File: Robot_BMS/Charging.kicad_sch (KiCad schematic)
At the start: 18 parts, among them Q7 2N7002, Q8 2N7002, Q9 2N7002, U4 MCP73833-xxx-MF, U5 MCP73833-xxx-MF, U6 MCP73833-xxx-MF

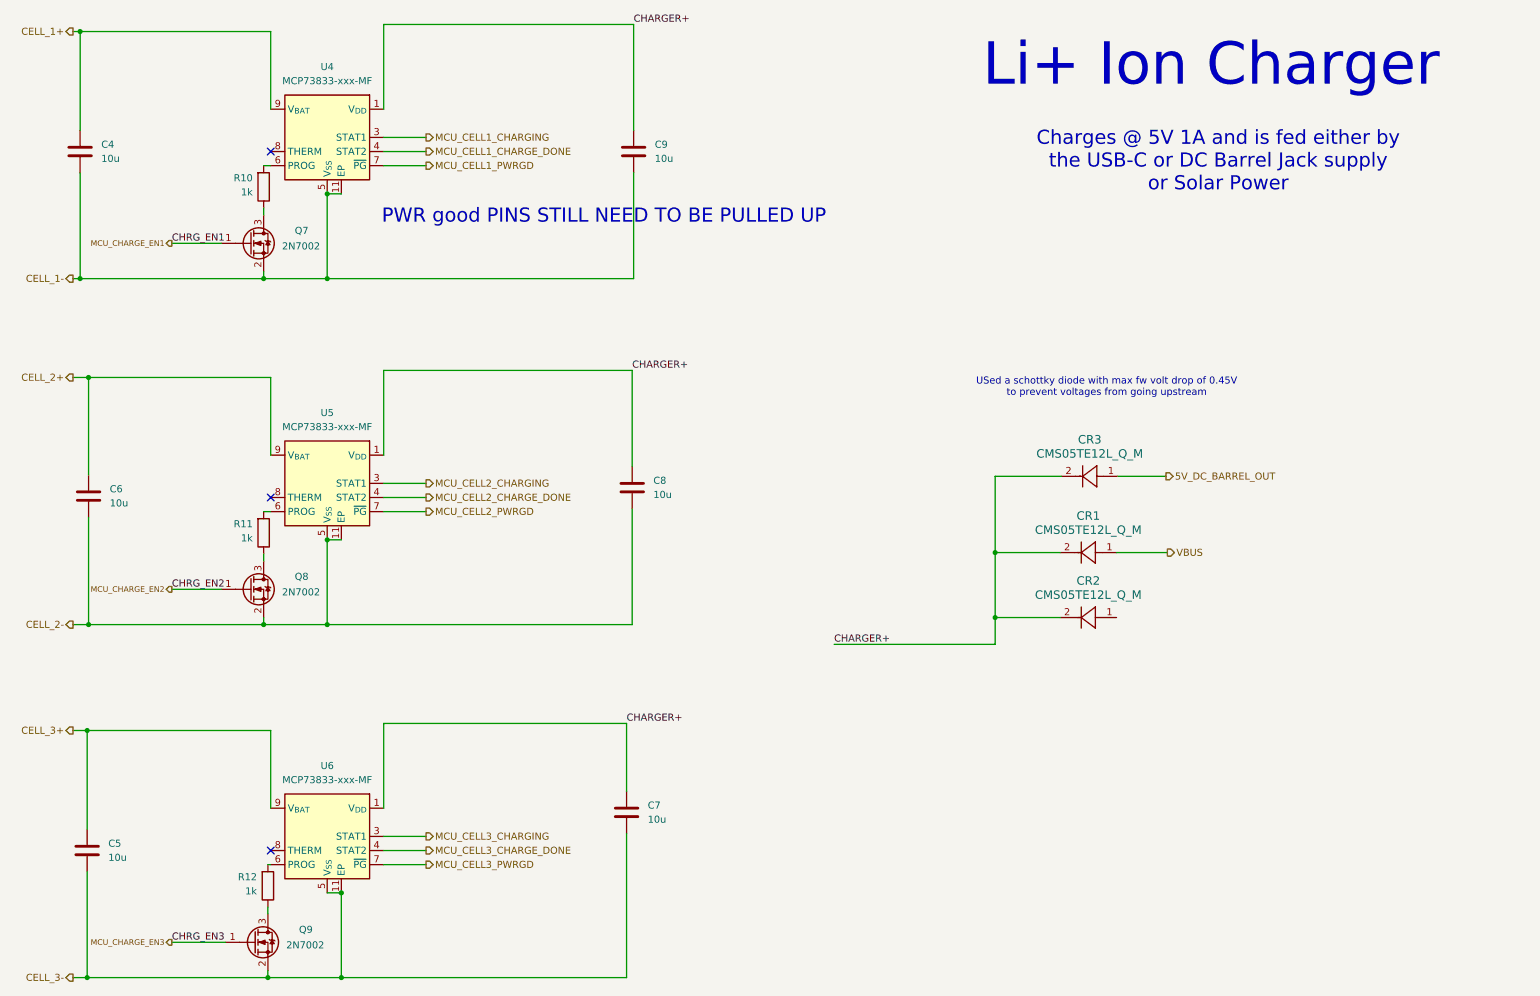
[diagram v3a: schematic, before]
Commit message: USB-c PD to 15V
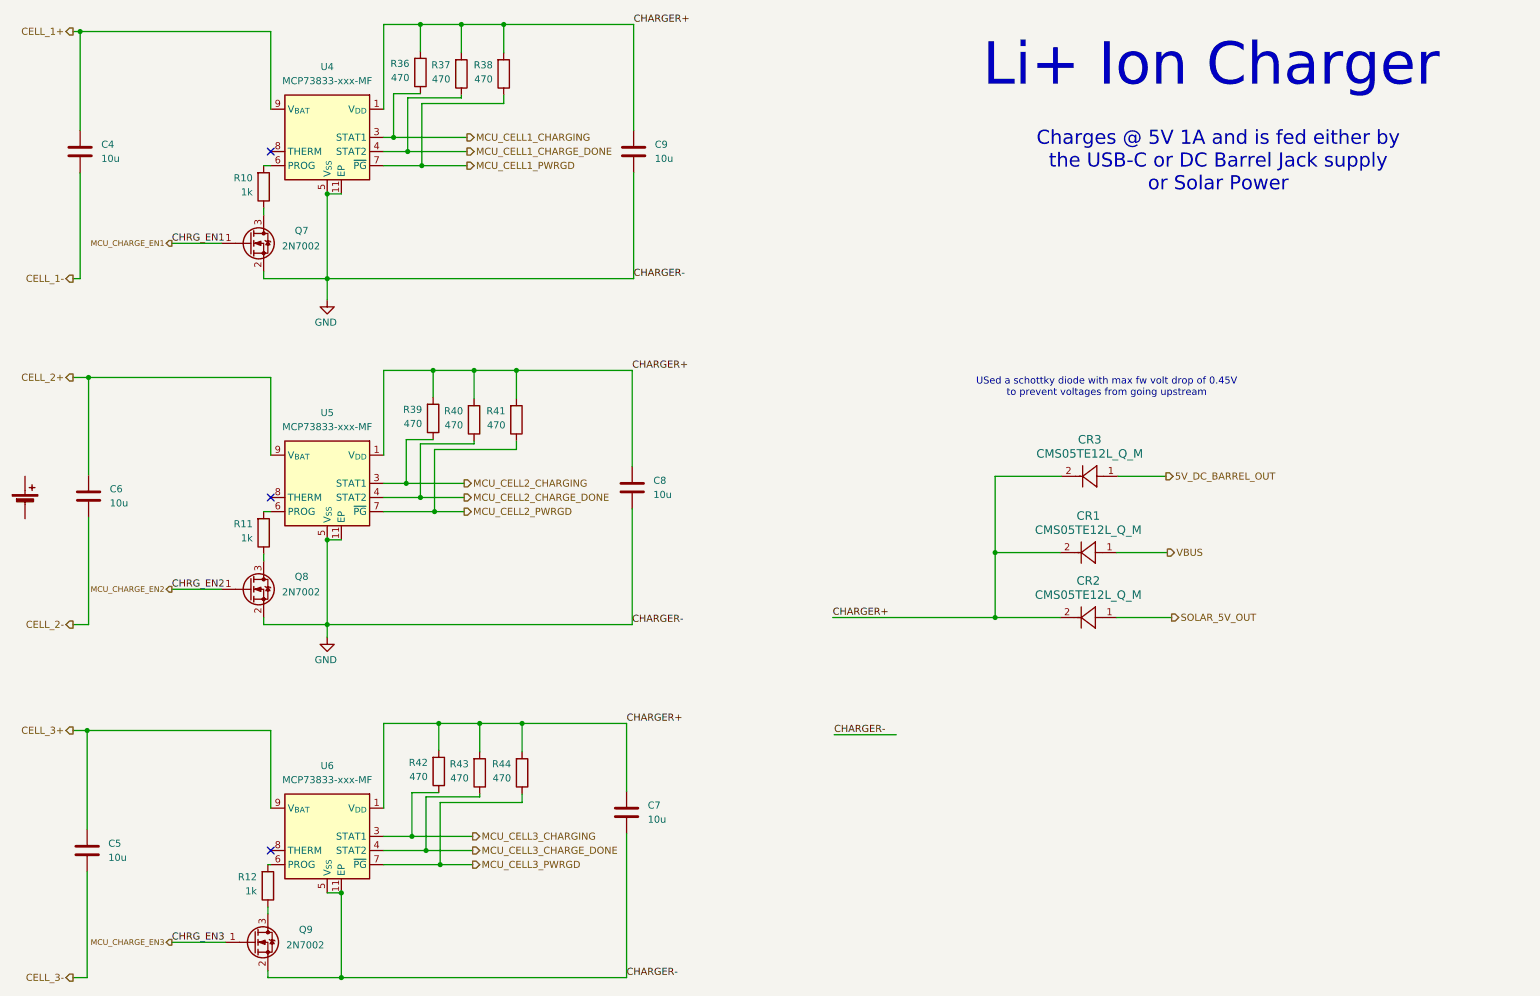
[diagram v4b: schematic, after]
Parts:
- added BT1: Battery_Cell, symbol Device:Battery_Cell
- added R36, R37, R38, R39, R40, R41, R42, R43, R44: 470, symbol Device:R
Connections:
- net CELL_1-: no longer C9.2, Q7.2 (S), U4.11 (EP), U4.5 (V_{SS})
- net CELL_2-: no longer C8.2, Q8.2 (S), U5.11 (EP), U5.5 (V_{SS})
- net CELL_3-: no longer C7.2, Q9.2 (S), U6.11 (EP), U6.5 (V_{SS})
- net CHARGER+: now also R36.2, R37.2, R38.2, R39.2, R40.2, R41.2, R42.2, R43.2, R44.2
- net MCU_CELL1_CHARGE_DONE: now also R37.1
- net MCU_CELL1_CHARGING: now also R36.1
- net MCU_CELL1_PWRGD: now also R38.1
- net MCU_CELL2_CHARGE_DONE: now also R40.1
- net MCU_CELL2_CHARGING: now also R39.1
- net MCU_CELL2_PWRGD: now also R41.1
- net MCU_CELL3_CHARGE_DONE: now also R43.1
- net MCU_CELL3_CHARGING: now also R42.1
- net MCU_CELL3_PWRGD: now also R44.1
- net SOLAR_5V_OUT: now reaches CR2.1
- new net GND: C7.2, C8.2, C9.2, Q7.2 (S), Q8.2 (S), Q9.2 (S), U4.11 (EP), U4.5 (V_{SS}), U5.11 (EP), U5.5 (V_{SS}), U6.11 (EP), U6.5 (V_{SS})
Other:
- note removed: "PWR good PINS STILL NEED TO BE PULLED UP"

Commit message: solar charger set to 15V
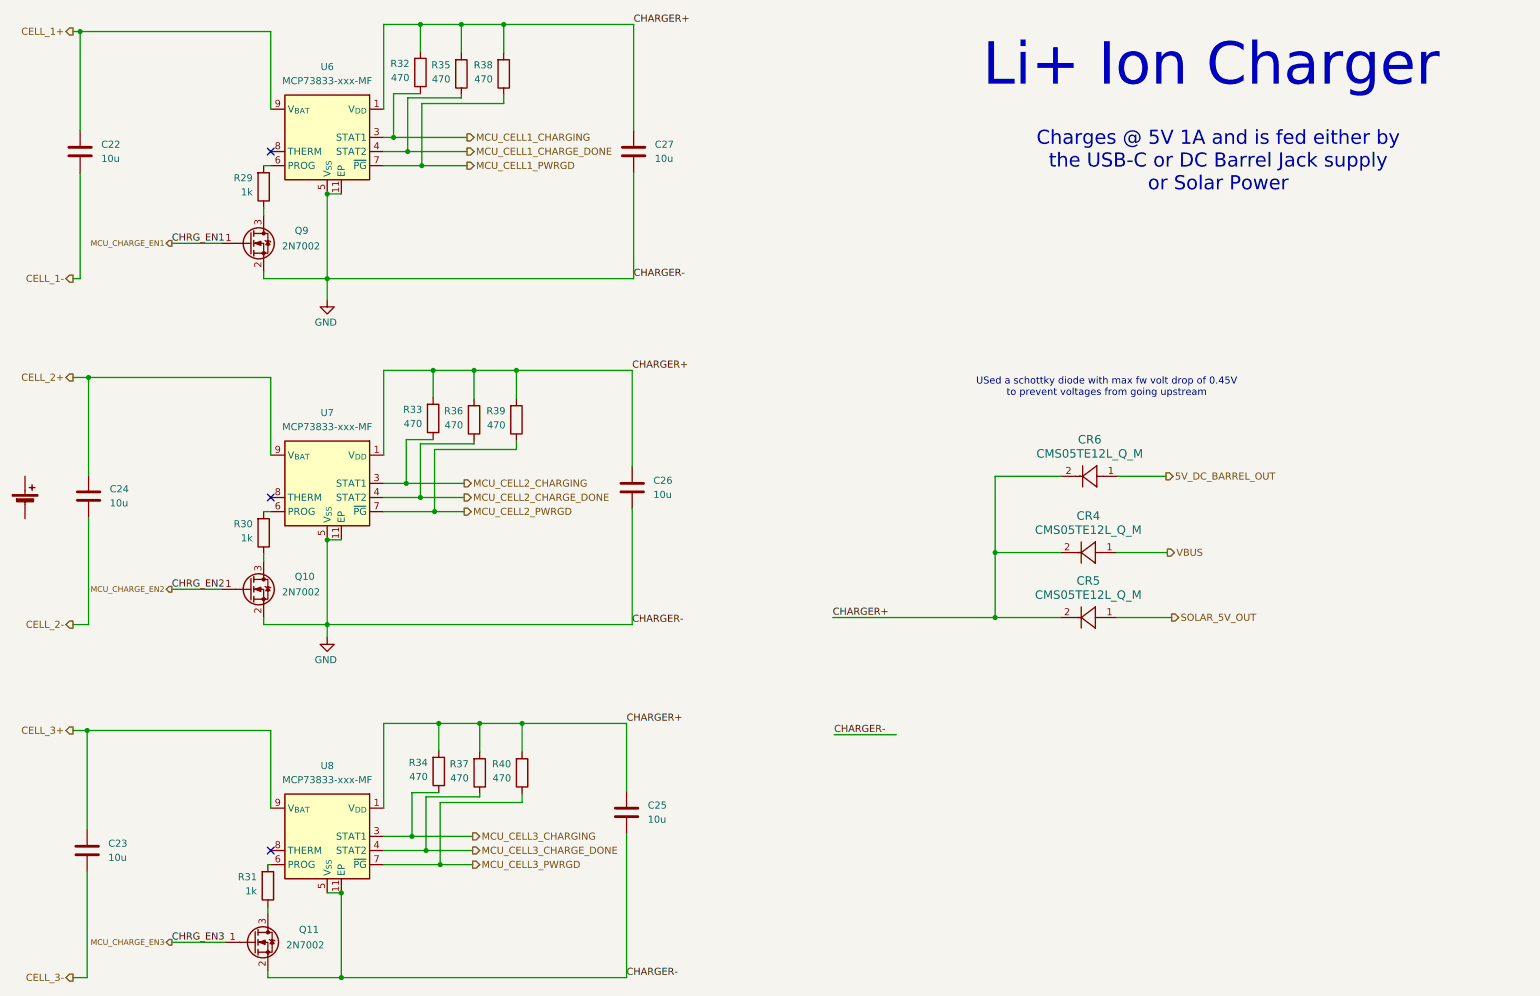
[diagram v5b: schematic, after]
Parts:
- renumbered C4 to C22, C5 to C23, C6 to C24, C7 to C25, C8 to C26, C9 to C27, CR1 to CR4, CR2 to CR5, CR3 to CR6, Q8 to Q10, Q9 to Q11, Q7 to Q9, R10 to R29, R11 to R30, R12 to R31, R36 to R32, R39 to R33, R42 to R34, R37 to R35, R40 to R36, R43 to R37, R41 to R39, R44 to R40, U4 to U6, U5 to U7, U6 to U8
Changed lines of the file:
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@@
 		(on_board yes)
 		(dnp no)
-		(property "Reference" "R39"
+		(property "Reference" "R33"
 			(at 88.2015 88.3285 0)
 			(effects
@@
 			(project "Robot_BMS"
 				(path "/72551b1c-3d40-4199-8911-e5b015f4abec/c0de399f-bcaa-40ff-9d4f-05779018e40a"
-					(reference "R39")
+					(reference "R33")
 					(unit 1)
 				)
@@
 		(on_board yes)
 		(dnp no)
-		(property "Reference" "R43"
+		(property "Reference" "R37"
 			(at 96.5835 152.0825 0)
 			(effects
@@
 			(project "Robot_BMS"
 				(path "/72551b1c-3d40-4199-8911-e5b015f4abec/c0de399f-bcaa-40ff-9d4f-05779018e40a"
-					(reference "R43")
+					(reference "R37")
 					(unit 1)
 				)
@@
 		(dnp no)
 		(fields_autoplaced yes)
-		(property "Reference" "C6"
+		(property "Reference" "C24"
 			(at 32.004 102.6159 0)
 			(effects
@@
 			(project "Robot_BMS"
 				(path "/72551b1c-3d40-4199-8911-e5b015f4abec/c0de399f-bcaa-40ff-9d4f-05779018e40a"
-					(reference "C6")
+					(reference "C24")
 					(unit 1)
 				)
@@
 		(dnp no)
 		(fields_autoplaced yes)
-		(property "Reference" "CR2"
+		(property "Reference" "CR5"
 			(at 208.026 119.126 0)
 			(effects
@@
 			(project "Robot_BMS"
 				(path "/72551b1c-3d40-4199-8911-e5b015f4abec/c0de399f-bcaa-40ff-9d4f-05779018e40a"
-					(reference "CR2")
+					(reference "CR5")
 					(unit 1)
 				)
@@
 		(on_board yes)
 		(dnp no)
-		(property "Reference" "U5"
+		(property "Reference" "U7"
 			(at 71.12 88.9 0)
 			(effects
@@
 			(project "Robot_BMS"
 				(path "/72551b1c-3d40-4199-8911-e5b015f4abec/c0de399f-bcaa-40ff-9d4f-05779018e40a"
-					(reference "U5")
+					(reference "U7")
 					(unit 1)
 				)
@@
 		(dnp no)
 		(fields_autoplaced yes)
-		(property "Reference" "C7"
+		(property "Reference" "C25"
 			(at 128.778 159.5119 0)
 			(effects
@@
 			(project "Robot_BMS"
 				(path "/72551b1c-3d40-4199-8911-e5b015f4abec/c0de399f-bcaa-40ff-9d4f-05779018e40a"
-					(reference "C7")
+					(reference "C25")
 					(unit 1)
 				)
@@
 		(on_board yes)
 		(dnp no)
-		(property "Reference" "R11"
+		(property "Reference" "R30"
 			(at 57.7215 108.9025 0)
 			(effects
@@
 			(project "Robot_BMS"
 				(path "/72551b1c-3d40-4199-8911-e5b015f4abec/c0de399f-bcaa-40ff-9d4f-05779018e40a"
-					(reference "R11")
+					(reference "R30")
 					(unit 1)
 				)
@@
 		(on_board yes)
 		(dnp no)
-		(property "Reference" "Q8"
+		(property "Reference" "Q10"
 			(at 65.278 118.364 0)
 			(effects
@@
 			(project "Robot_BMS"
 				(path "/72551b1c-3d40-4199-8911-e5b015f4abec/c0de399f-bcaa-40ff-9d4f-05779018e40a"
-					(reference "Q8")
+					(reference "Q10")
 					(unit 1)
 				)
@@
 		(dnp no)
 		(fields_autoplaced yes)
-		(property "Reference" "CR3"
+		(property "Reference" "CR6"
 			(at 208.28 93.726 0)
 			(effects
@@
 			(project ""
 				(path "/72551b1c-3d40-4199-8911-e5b015f4abec/c0de399f-bcaa-40ff-9d4f-05779018e40a"
-					(reference "CR3")
+					(reference "CR6")
 					(unit 1)
 				)
@@
 		(on_board yes)
 		(dnp no)
-		(property "Reference" "#PWR033"
+		(property "Reference" "#PWR035"
 			(at 71.12 74.93 0)
 			(effects
@@
 			(project "Robot_BMS"
 				(path "/72551b1c-3d40-4199-8911-e5b015f4abec/c0de399f-bcaa-40ff-9d4f-05779018e40a"
-					(reference "#PWR033")
+					(reference "#PWR035")
 					(unit 1)
 				)
@@
 		(on_board yes)
 		(dnp no)
-		(property "Reference" "R40"
+		(property "Reference" "R36"
 			(at 95.5675 88.5825 0)
 			(effects
@@
 			(project "Robot_BMS"
 				(path "/72551b1c-3d40-4199-8911-e5b015f4abec/c0de399f-bcaa-40ff-9d4f-05779018e40a"
-					(reference "R40")
+					(reference "R36")
 					(unit 1)
 				)
@@
 		(on_board yes)
 		(dnp no)
-		(property "Reference" "U6"
+		(property "Reference" "U8"
 			(at 71.12 152.4 0)
 			(effects
@@
 			(project "Robot_BMS"
 				(path "/72551b1c-3d40-4199-8911-e5b015f4abec/c0de399f-bcaa-40ff-9d4f-05779018e40a"
-					(reference "U6")
+					(reference "U8")
 					(unit 1)
 				)
@@
 		(dnp no)
 		(fields_autoplaced yes)
-		(property "Reference" "C5"
+		(property "Reference" "C23"
 			(at 31.75 166.3699 0)
 			(effects
@@
 			(project "Robot_BMS"
 				(path "/72551b1c-3d40-4199-8911-e5b015f4abec/c0de399f-bcaa-40ff-9d4f-05779018e40a"
-					(reference "C5")
+					(reference "C23")
 					(unit 1)
 				)
@@
 		(on_board yes)
 		(dnp no)
-		(property "Reference" "R10"
+		(property "Reference" "R29"
 			(at 57.7215 46.6725 0)
 			(effects
@@
 			(project "Robot_BMS"
 				(path "/72551b1c-3d40-4199-8911-e5b015f4abec/c0de399f-bcaa-40ff-9d4f-05779018e40a"
-					(reference "R10")
+					(reference "R29")
 					(unit 1)
 				)
@@
 		(on_board yes)
 		(dnp no)
-		(property "Reference" "R12"
+		(property "Reference" "R31"
 			(at 58.4835 172.4025 0)
 			(effects
@@
 			(project "Robot_BMS"
 				(path "/72551b1c-3d40-4199-8911-e5b015f4abec/c0de399f-bcaa-40ff-9d4f-05779018e40a"
-					(reference "R12")
+					(reference "R31")
 					(unit 1)
 				)
@@
 		(on_board yes)
 		(dnp no)
-		(property "Reference" "Q7"
+		(property "Reference" "Q9"
 			(at 65.278 56.134 0)
 			(effects
@@
 			(project "Robot_BMS"
 				(path "/72551b1c-3d40-4199-8911-e5b015f4abec/c0de399f-bcaa-40ff-9d4f-05779018e40a"
-					(reference "Q7")
+					(reference "Q9")
 					(unit 1)
 				)
@@
 		(on_board yes)
 		(dnp no)
-		(property "Reference" "R44"
+		(property "Reference" "R40"
 			(at 104.2035 152.0825 0)
 			(effects
@@
 			(project "Robot_BMS"
 				(path "/72551b1c-3d40-4199-8911-e5b015f4abec/c0de399f-bcaa-40ff-9d4f-05779018e40a"
-					(reference "R44")
+					(reference "R40")
 					(unit 1)
 				)
@@
 		(on_board yes)
 		(dnp no)
-		(property "Reference" "R36"
+		(property "Reference" "R32"
 			(at 85.9155 26.0985 0)
 			(effects
@@
 			(project "Robot_BMS"
 				(path "/72551b1c-3d40-4199-8911-e5b015f4abec/c0de399f-bcaa-40ff-9d4f-05779018e40a"
-					(reference "R36")
+					(reference "R32")
 					(unit 1)
 				)
@@
 		(on_board yes)
 		(dnp no)
-		(property "Reference" "#PWR034"
+		(property "Reference" "#PWR036"
 			(at 71.12 135.636 0)
 			(effects
@@
 			(project "Robot_BMS"
 				(path "/72551b1c-3d40-4199-8911-e5b015f4abec/c0de399f-bcaa-40ff-9d4f-05779018e40a"
-					(reference "#PWR034")
+					(reference "#PWR036")
 					(unit 1)
 				)
@@
 		(dnp no)
 		(fields_autoplaced yes)
-		(property "Reference" "C4"
+		(property "Reference" "C22"
 			(at 30.48 40.6399 0)
 			(effects
@@
 			(project "Robot_BMS"
 				(path "/72551b1c-3d40-4199-8911-e5b015f4abec/c0de399f-bcaa-40ff-9d4f-05779018e40a"
-					(reference "C4")
+					(reference "C22")
 					(unit 1)
 				)
@@
 		(on_board yes)
 		(dnp no)
-		(property "Reference" "Q9"
+		(property "Reference" "Q11"
 			(at 66.04 181.864 0)
 			(effects
@@
 			(project "Robot_BMS"
 				(path "/72551b1c-3d40-4199-8911-e5b015f4abec/c0de399f-bcaa-40ff-9d4f-05779018e40a"
-					(reference "Q9")
+					(reference "Q11")
 					(unit 1)
 				)
@@
 		(on_board yes)
 		(dnp no)
-		(property "Reference" "R42"
+		(property "Reference" "R34"
 			(at 89.2175 151.8285 0)
 			(effects
@@
 			(project "Robot_BMS"
 				(path "/72551b1c-3d40-4199-8911-e5b015f4abec/c0de399f-bcaa-40ff-9d4f-05779018e40a"
-					(reference "R42")
+					(reference "R34")
 					(unit 1)
 				)
@@
 		(on_board yes)
 		(dnp no)
-		(property "Reference" "U4"
+		(property "Reference" "U6"
 			(at 71.12 26.67 0)
 			(effects
@@
 			(project "Robot_BMS"
 				(path "/72551b1c-3d40-4199-8911-e5b015f4abec/c0de399f-bcaa-40ff-9d4f-05779018e40a"
-					(reference "U4")
+					(reference "U6")
 					(unit 1)
 				)
@@
 		(dnp no)
 		(fields_autoplaced yes)
-		(property "Reference" "C9"
+		(property "Reference" "C27"
 			(at 130.048 40.6399 0)
 			(effects
@@
 			(project "Robot_BMS"
 				(path "/72551b1c-3d40-4199-8911-e5b015f4abec/c0de399f-bcaa-40ff-9d4f-05779018e40a"
-					(reference "C9")
+					(reference "C27")
 					(unit 1)
 				)
@@
 		(on_board yes)
 		(dnp no)
-		(property "Reference" "R37"
+		(property "Reference" "R35"
 			(at 93.2815 26.3525 0)
 			(effects
@@
 			(project "Robot_BMS"
 				(path "/72551b1c-3d40-4199-8911-e5b015f4abec/c0de399f-bcaa-40ff-9d4f-05779018e40a"
-					(reference "R37")
+					(reference "R35")
 					(unit 1)
 				)
@@
 		(dnp no)
 		(fields_autoplaced yes)
-		(property "Reference" "CR1"
+		(property "Reference" "CR4"
 			(at 208.026 107.442 0)
 			(effects
@@
 			(project "Robot_BMS"
 				(path "/72551b1c-3d40-4199-8911-e5b015f4abec/c0de399f-bcaa-40ff-9d4f-05779018e40a"
-					(reference "CR1")
+					(reference "CR4")
 					(unit 1)
 				)
@@
 		(dnp no)
 		(fields_autoplaced yes)
-		(property "Reference" "C8"
+		(property "Reference" "C26"
 			(at 129.794 101.0919 0)
 			(effects
@@
 			(project "Robot_BMS"
 				(path "/72551b1c-3d40-4199-8911-e5b015f4abec/c0de399f-bcaa-40ff-9d4f-05779018e40a"
-					(reference "C8")
+					(reference "C26")
 					(unit 1)
 				)
@@
 		(on_board yes)
 		(dnp no)
-		(property "Reference" "R41"
+		(property "Reference" "R39"
 			(at 103.1875 88.5825 0)
 			(effects
@@
 			(project "Robot_BMS"
 				(path "/72551b1c-3d40-4199-8911-e5b015f4abec/c0de399f-bcaa-40ff-9d4f-05779018e40a"
-					(reference "R41")
-					(unit 1)
-				)
+					(reference "R39")
+					(unit 1)
+				)

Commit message: ex charging circuit last appearence
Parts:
- added BT2: Battery_Cell, symbol Device:Battery_Cell
- renumbered C22 to C28, C23 to C29, C24 to C30, C25 to C31, C26 to C32, C27 to C33, Q11 to Q10, Q9 to Q8, Q10 to Q9, R29 to R33, R30 to R34, R31 to R35, R32 to R36, R33 to R37, R34 to R38, R35 to R39, R36 to R40, R37 to R41, R38 to R42, R39 to R43, R40 to R44, U6 to U7, U7 to U8, U8 to U9
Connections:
- net at BT1.1 (+): now also BT2.2 (-)
